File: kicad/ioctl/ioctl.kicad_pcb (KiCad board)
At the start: 2 copper layers, 33 parts, among them P1 CONN_01X08, P2 CONN_01X08, P3 CONN_01X03, P4 CONN_02X04, P5 CONN_02X04, P7 CONN_01X08, P8 CONN_02X03, P9 CONN_01X08, U1 74922, U2 74922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

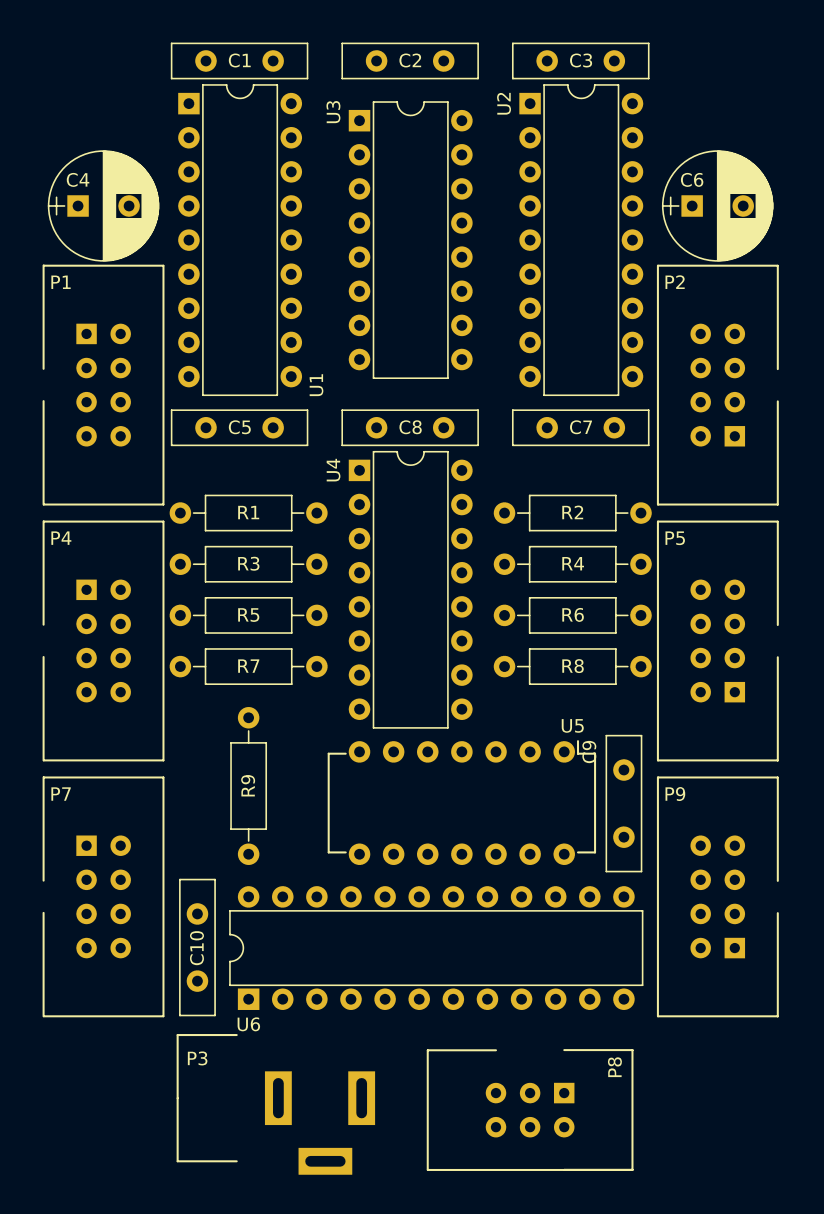
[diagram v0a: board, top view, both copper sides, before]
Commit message: Add mounting holes to the IO Controller PCB
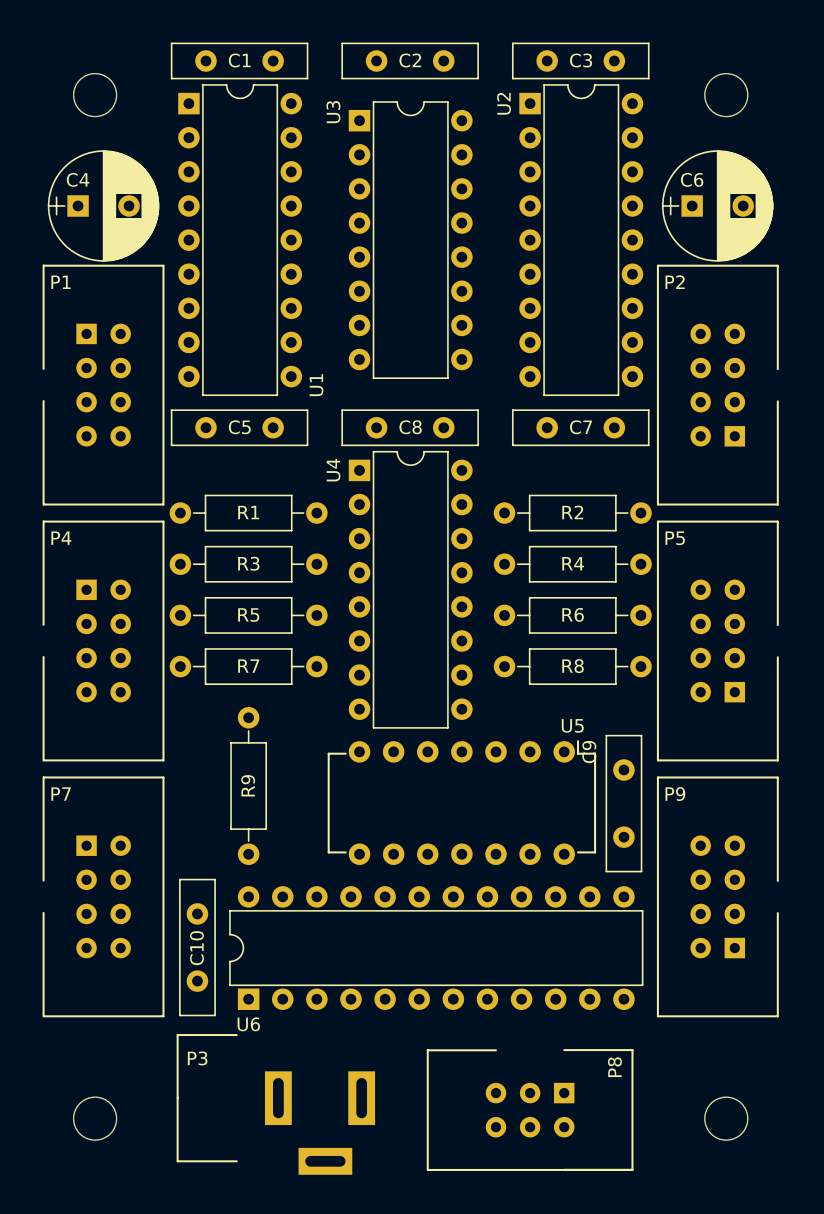
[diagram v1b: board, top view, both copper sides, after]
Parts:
- added REF**: Hole, avionica:MountingHole_M3, F.Cu at (180.3, 35.6)
- added REF**: Hole, avionica:MountingHole_M3, F.Cu at (227.3, 35.6)
- added REF**: Hole, avionica:MountingHole_M3, F.Cu at (180.3, 111.8)
- added REF**: Hole, avionica:MountingHole_M3, F.Cu at (227.3, 111.8)
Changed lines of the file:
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@@
 (kicad_pcb (version 4) (host pcbnew 4.0.7)
   (general
-    (links 130)
+    (links 0)
     (no_connects 130)
-    (area 176.229999 31.194999 231.440001 116.135)
+    (area 175.159999 30.379999 232.510001 116.940001)
     (thickness 1.6)
     (drawings 4)
     (tracks 0)
     (zones 0)
-    (modules 33)
+    (modules 37)
     (nets 62)
   )
@@
     )
   )
-  (module avionica:Disc_capacitor (layer F.Cu)
+  (module avionica:Disc_capacitor locked (layer F.Cu)
     (at 188.595 33.02)
     (descr "C, Disc series, Radial, pin pitch=5.00mm, , diameter*width=10*2.5mm^2, Capacitor, http://cdn-reichelt.de/documents/datenblatt/B300/DS_KERKO_TC.pdf")
@@
     )
   )
+  (module avionica:MountingHole_M3 (layer F.Cu)
+    (at 180.34 35.56)
+    (descr "Mounting Hole 3.2mm, no annular, M3")
+    (tags "mounting hole 3.2mm no annular m3")
+    (fp_text reference REF** (at 0 -1.27) (layer F.SilkS) hide
+      (effects (font (size 1 1) (thickness 0.15)))
+    )
+    (fp_text value Hole (at 0 1.27) (layer F.Fab) hide
+      (effects (font (size 1 1) (thickness 0.15)))
+    )
+    (fp_circle (center 0 0) (end 3.2 0) (layer Cmts.User) (width 0.15))
+    (fp_circle (center 0 0) (end 3.45 0) (layer F.CrtYd) (width 0.05))
+    (pad 1 np_thru_hole circle (at 0 0) (size 3.2 3.2) (drill 3.2) (layers *.Cu *.Mask))
+  )
+  (module avionica:MountingHole_M3 (layer F.Cu)
+    (at 227.33 35.56)
+    (descr "Mounting Hole 3.2mm, no annular, M3")
+    (tags "mounting hole 3.2mm no annular m3")
+    (fp_text reference REF** (at 0 -1.27) (layer F.SilkS) hide
+      (effects (font (size 1 1) (thickness 0.15)))
+    )
+    (fp_text value Hole (at 0 1.27) (layer F.Fab) hide
+      (effects (font (size 1 1) (thickness 0.15)))
+    )
+    (fp_circle (center 0 0) (end 3.2 0) (layer Cmts.User) (width 0.15))
+    (fp_circle (center 0 0) (end 3.45 0) (layer F.CrtYd) (width 0.05))
+    (pad 1 np_thru_hole circle (at 0 0) (size 3.2 3.2) (drill 3.2) (layers *.Cu *.Mask))
+  )
+  (module avionica:MountingHole_M3 (layer F.Cu)
+    (at 180.34 111.76)
+    (descr "Mounting Hole 3.2mm, no annular, M3")
+    (tags "mounting hole 3.2mm no annular m3")
+    (fp_text reference REF** (at 0 -1.27) (layer F.SilkS) hide
+      (effects (font (size 1 1) (thickness 0.15)))
+    )
+    (fp_text value Hole (at 0 1.27) (layer F.Fab) hide
+      (effects (font (size 1 1) (thickness 0.15)))
+    )
+    (fp_circle (center 0 0) (end 3.2 0) (layer Cmts.User) (width 0.15))
+    (fp_circle (center 0 0) (end 3.45 0) (layer F.CrtYd) (width 0.05))
+    (pad 1 np_thru_hole circle (at 0 0) (size 3.2 3.2) (drill 3.2) (layers *.Cu *.Mask))
+  )
+  (module avionica:MountingHole_M3 (layer F.Cu)
+    (at 227.33 111.76)
+    (descr "Mounting Hole 3.2mm, no annular, M3")
+    (tags "mounting hole 3.2mm no annular m3")
+    (fp_text reference REF** (at 0 -1.27) (layer F.SilkS) hide
+      (effects (font (size 1 1) (thickness 0.15)))
+    )
+    (fp_text value Hole (at 0 1.27) (layer F.Fab) hide
+      (effects (font (size 1 1) (thickness 0.15)))
+    )
+    (fp_circle (center 0 0) (end 3.2 0) (layer Cmts.User) (width 0.15))
+    (fp_circle (center 0 0) (end 3.45 0) (layer F.CrtYd) (width 0.05))
+    (pad 1 np_thru_hole circle (at 0 0) (size 3.2 3.2) (drill 3.2) (layers *.Cu *.Mask))
+  )
   (gr_line (start 175.26 116.84) (end 175.26 30.48) (angle 90) (layer Margin) (width 0.2))

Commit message: Add several layers in silkscreen for IO Controller board PCB
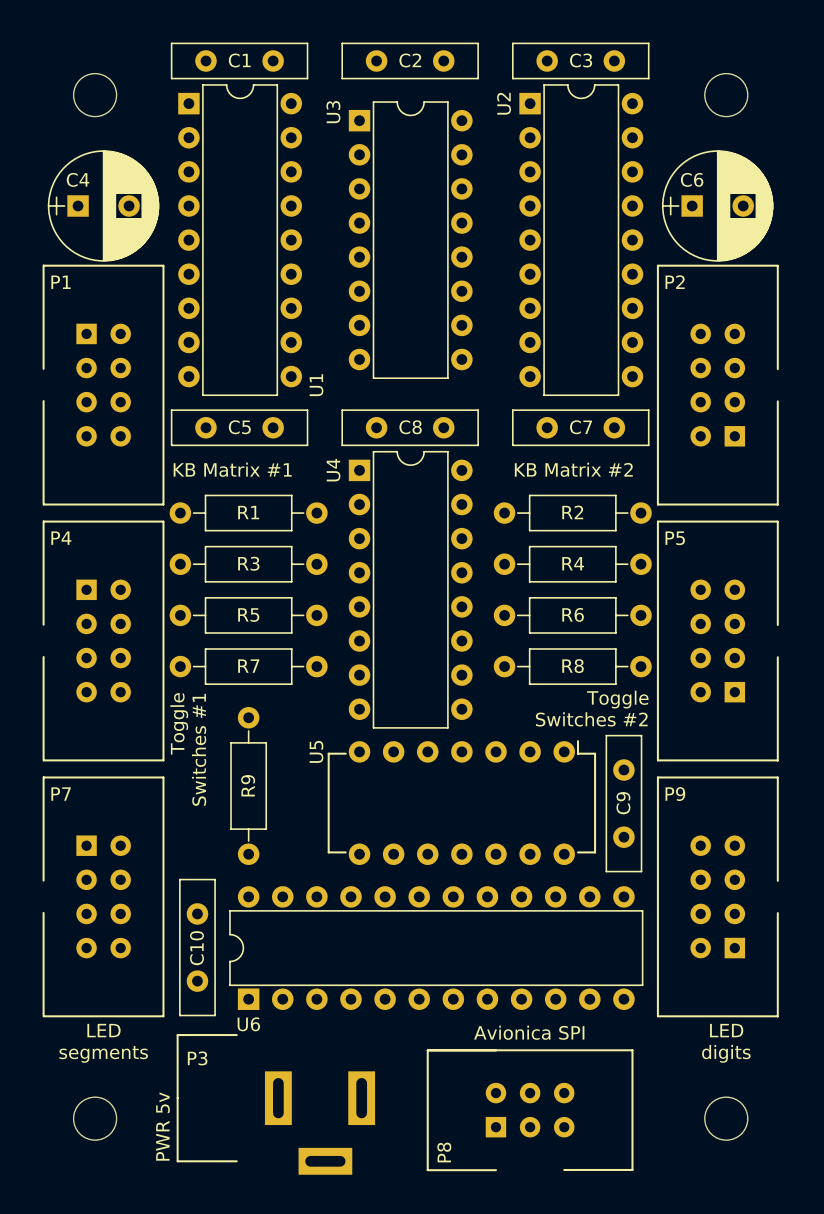
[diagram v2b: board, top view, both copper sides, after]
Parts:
- moved P8 5.68 mm to (210.2, 112.4), turned to 90 degrees
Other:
- board text added: "Avionica IO Controller Board Rev01"
- board text added: "Avionica SPI"
- board text added: "Copyright (C) 2017 Alvaro Polo"
- board text added: "KB Matrix #1"
- board text added: "KB Matrix #2"
- board text added: "LED digits"
- board text added: "LED segments"
- board text added: "PWR 5v"
- board text added: "Toggle Switches #1"
- board text added: "Toggle Switches #2"

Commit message: Use a single IDC10 connector for switches in IO Controller board
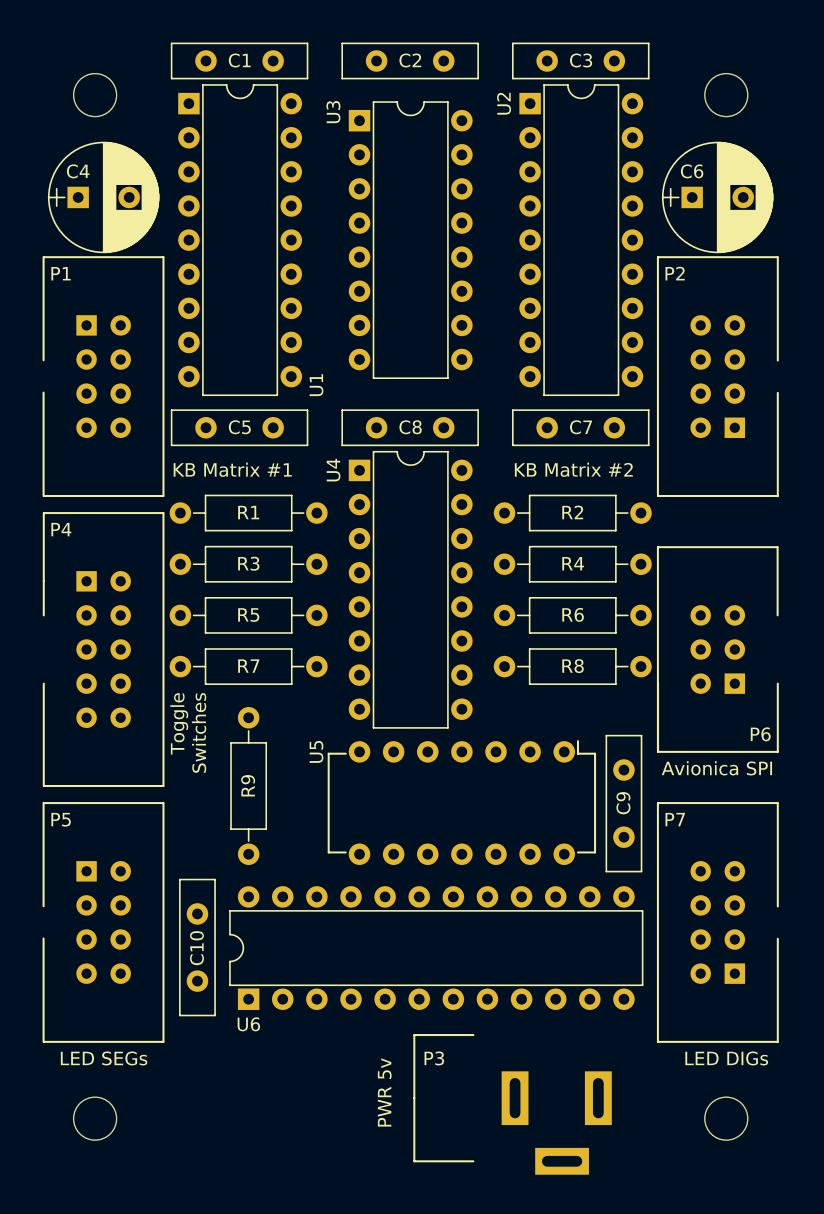
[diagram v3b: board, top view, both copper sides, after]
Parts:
- removed the P5 at (228.0, 80.0)
- P4: value CONN_02X04 -> CONN_02X05; footprint avionica:idc-8p -> avionica:idc-10p
- moved P6 37.5 mm to (228.0, 79.4), turned to 180 degrees
- moved P3 17.6 mm to (215.1, 114.9)
- moved P5 1.91 mm to (179.7, 93.3)
- moved P7 1.91 mm to (228.0, 101.0)
- moved C4 0.64 mm to (179.1, 43.2)
- moved P1 0.64 mm to (179.7, 52.7)
- moved P4 0.64 mm to (179.7, 71.8)
- moved C6 0.63 mm to (224.8, 43.2)
- moved P2 0.63 mm to (228.0, 60.3)
- renumbered P7 to P5, P8 to P6, P9 to P7
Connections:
- P4 pad 1: VCC -> Net-(P4-Pad1)
- P4 pad 3: VCC -> Net-(P4-Pad3)
- P4 pad 5: VCC -> Net-(P4-Pad5)
- P4 pad 7: VCC -> Net-(P4-Pad7)
- R1 pad 1: Net-(P4-Pad8) -> Net-(P4-Pad1)
- R2 pad 1: Net-(P5-Pad2) -> Net-(P4-Pad2)
- R3 pad 1: Net-(P4-Pad6) -> Net-(P4-Pad3)
- R4 pad 1: Net-(P5-Pad4) -> Net-(P4-Pad4)
- R5 pad 1: Net-(P4-Pad4) -> Net-(P4-Pad5)
- R6 pad 1: Net-(P5-Pad6) -> Net-(P4-Pad6)
- R7 pad 1: Net-(P4-Pad2) -> Net-(P4-Pad7)
- R8 pad 1: Net-(P5-Pad8) -> Net-(P4-Pad8)
- U4 pad 1: Net-(P5-Pad8) -> Net-(P4-Pad8)
- U4 pad 13: Net-(P5-Pad2) -> Net-(P4-Pad2)
- U4 pad 14: Net-(P5-Pad4) -> Net-(P4-Pad4)
- U4 pad 15: Net-(P5-Pad6) -> Net-(P4-Pad6)
- U4 pad 4: Net-(P4-Pad8) -> Net-(P4-Pad1)
- U4 pad 5: Net-(P4-Pad6) -> Net-(P4-Pad3)
- U4 pad 6: Net-(P4-Pad4) -> Net-(P4-Pad5)
- U4 pad 7: Net-(P4-Pad2) -> Net-(P4-Pad7)
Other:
- board text added: "LED DIGs"
- board text added: "LED SEGs"
- board text added: "Toggle Switches"
- board text removed: "LED digits"
- board text removed: "LED segments"
- board text removed: "Toggle Switches #1"
- board text removed: "Toggle Switches #2"

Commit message: Complete connections of IO Controller board PCB
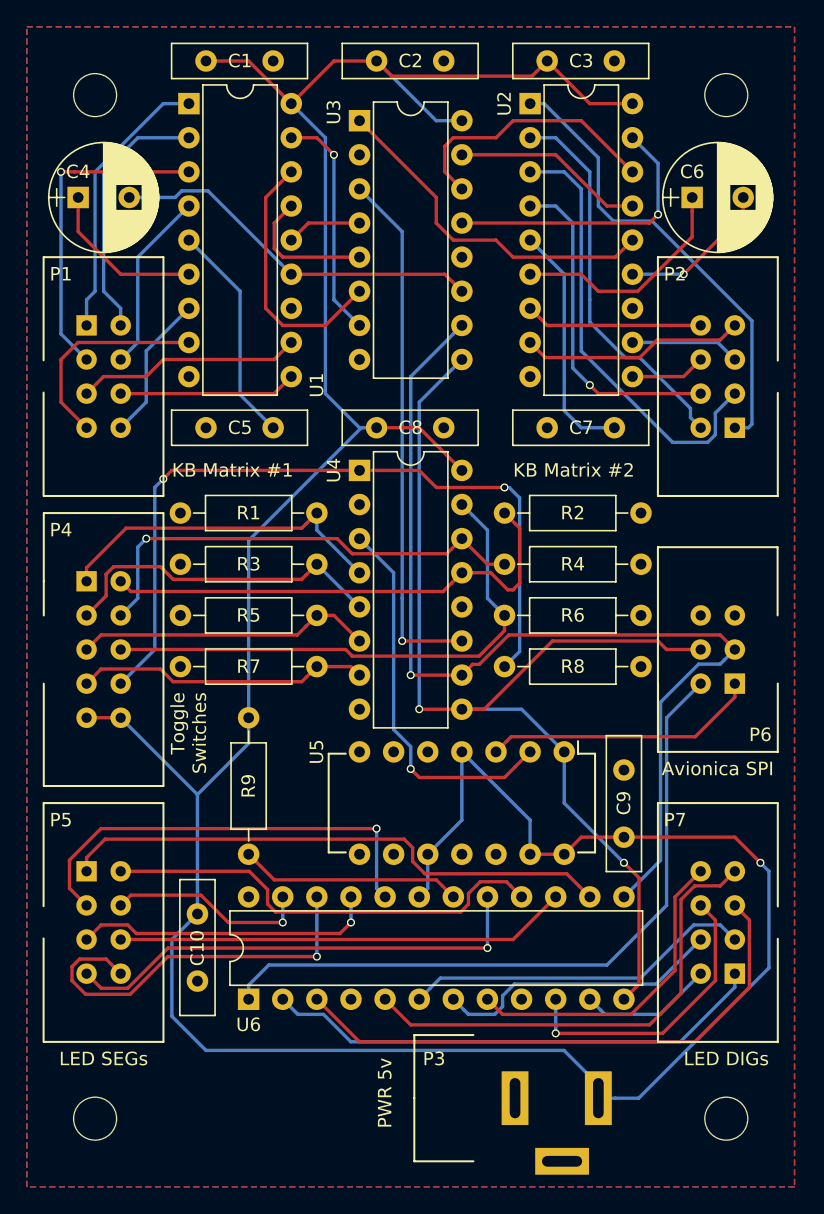
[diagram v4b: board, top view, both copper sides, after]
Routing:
- net VCC: track 0.00 -> 240.2 mm, vias 0 -> 1
- net ~SS: track 0.00 -> 80.8 mm, vias 0 -> 2
- net SCK: track 0.00 -> 76.2 mm, vias 0 -> 1
- net Net-(P4-Pad8): track 0.00 -> 57.2 mm, vias 0 -> 2
- net MOSI: track 0.00 -> 52.2 mm
- net Net-(P9-Pad5): track 0.00 -> 41.8 mm
- net Net-(P7-Pad1): track 0.00 -> 41.4 mm
- net Net-(P4-Pad6): track 0.00 -> 40.3 mm
- net GND: track 0.00 -> 39.4 mm, vias 0 -> 1
- net Net-(U3-Pad3): track 0.00 -> 39.4 mm, vias 0 -> 1
- net Net-(P9-Pad1): track 0.00 -> 37.7 mm
- net Net-(P4-Pad2): track 0.00 -> 37.0 mm
- net Net-(P9-Pad7): track 0.00 -> 35.6 mm
- net Net-(P7-Pad7): track 0.00 -> 35.3 mm, vias 0 -> 1
- net Net-(P4-Pad4): track 0.00 -> 34.9 mm, vias 0 -> 1
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- added copper zone on B.Cu, net GND
- added copper zone on F.Cu, net GND

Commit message: Add OSHW logo to IO Controller board and fix some labels
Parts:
- added REF***: Logo, avionica:logo-oshw, B.Cu at (227.3, 67.9)
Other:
- board text added: "Avionica Project IO Controller Board Rev01 Copyright (C) 2017 Alvaro Polo"
- board text removed: "Avionica IO Controller Board Rev01"
- board text removed: "Copyright (C) 2017 Alvaro Polo"

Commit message: Use more appropriate models for capacitor footprints
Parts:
- moved C2 2.54 mm to (203.8, 33.0)
- moved C8 2.54 mm to (203.8, 60.3)
- moved C10 2.54 mm to (188.0, 99.1)
- moved C9 2.54 mm to (219.7, 88.3)
- moved C1 2.54 mm to (191.1, 33.0)
- moved C3 2.54 mm to (216.5, 33.0)
- moved C5 2.54 mm to (191.1, 60.3)
- moved C7 2.54 mm to (216.5, 60.3)
- moved C6 2.18 mm to (227.0, 43.2), turned to 270 degrees
- moved C4 1.62 mm to (180.7, 43.2), turned to 270 degrees
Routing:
- net Net-(P1-Pad2): track 19.4 -> 23.3 mm
- net Net-(P1-Pad1): track 20.8 -> 24.2 mm
- net GND: track 39.4 -> 40.3 mm
- net Net-(P1-Pad3): track 24.3 -> 25.2 mm
- net Net-(C6-Pad1): track 17.2 -> 17.8 mm
